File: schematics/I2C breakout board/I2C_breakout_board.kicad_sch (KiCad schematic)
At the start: 22 parts, among them J1 Conn_01x01_Pin, J10 Conn_01x01_Pin, J11 Conn_01x01_Pin, J12 Conn_01x01_Pin, J13 Conn_01x01_Pin, J14 Conn_01x01_Pin, J15 Conn_01x01_Pin, J16 Conn_01x01_Pin, J17 Conn_01x01_Pin, J2 Conn_01x01_Pin, J3 Conn_01x01_Pin, J4 Conn_01x01_Pin, J5 Conn_01x01_Pin, J6 Conn_01x01_Pin, J7 Conn_01x01_Pin, J8 Conn_01x01_Pin, J9 Conn_01x01_Pin, U1 ENS210-LQFM, U2 OPT4001DTSR

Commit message: testing how to make branches, added dummy text to the schematic
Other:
- note added: "DUMMY TEXT FOR MAKING A BRANCH on github"
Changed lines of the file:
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@@
 		(company "RES-Q-SQUAD")
+	)
+	(text "DUMMY TEXT FOR MAKING A BRANCH\non github\n"
+		(exclude_from_sim no)
+		(at 229.616 59.182 0)
+		(effects
+			(font
+				(size 1.27 1.27)
+			)
+		)
 	)
 	(junction

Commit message: updated schematic
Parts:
- removed J1, J10, J11, J12, J13, J14, J15, J16, J17, J2, J3, J4, J5, J6, J7, J8, J9: Conn_01x01_Pin, Connector_PinHeader_2.54mm:PinHeader_1x01_P2.54mm_Vertical, symbol Connector:Conn_01x01_Pin
- added J1, J2: Conn_01x07_Pin, Connector_PinHeader_2.54mm:PinHeader_1x07_P2.54mm_Vertical, symbol Connector:Conn_01x07_Pin
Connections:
- net +3.3V: now also J1.1 (Pin_1), J2.7 (Pin_7)
- net GND: now also J2.1 (Pin_1), J2.6 (Pin_6)
- net SCL: now reaches U1.2 (SCL)
- net SCL: now also U2.5 (SCL), J1.2 (Pin_2)
- net SDA: now reaches U1.3 (SDA)
- net SDA: now also U2.8 (SDA), J2.2 (Pin_2)
- net U3_DI: now reaches U3.4 (DI)
- net U3_DI: now also J1.7 (Pin_7)
- net U3_RO: now reaches U3.1 (RO)
- net U3_RO: now also J1.4 (Pin_4)
- net U2_ADDR: now reaches U2.2 (ADDR)
- net U2_ADDR: now also J1.3 (Pin_3)
- net U2_INT: now reaches U2.7 (INT)
- net U2_INT: now also J2.3 (Pin_3)
- net U3_DE: now reaches U3.3 (DE)
- net U3_DE: now also J1.6 (Pin_6)
- net U3_/RE: now reaches U3.2 (/RE)
- net U3_/RE: now also J1.5 (Pin_5)
- net U3__B: now reaches U3.7 (B)
- net U3__B: now also J2.4 (Pin_4)
- net U3_A: now reaches U3.6 (A)
- net U3_A: now also J2.5 (Pin_5)
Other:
- moved on the sheet: C1, C2

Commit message: finalized PCB for breakout board
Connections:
- net +3.3V: now also J2.4 (Pin_4); no longer J2.7 (Pin_7)
- net GND: now also J1.2 (Pin_2), J2.7 (Pin_7); no longer J2.1 (Pin_1), J2.6 (Pin_6)
- net SCL: now also J2.2 (Pin_2); no longer J1.2 (Pin_2)
- net SDA: now also J2.1 (Pin_1); no longer J2.2 (Pin_2)
- net U2_ADDR: now also J2.3 (Pin_3); no longer J1.3 (Pin_3)
- net U2_INT: now also J1.3 (Pin_3); no longer J2.3 (Pin_3)
- net U3_A: now also J2.6 (Pin_6); no longer J2.5 (Pin_5)
- net U3__B: now also J2.5 (Pin_5); no longer J2.4 (Pin_4)

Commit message: .
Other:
- note removed: "DUMMY TEXT FOR MAKING A BRANCH on github"
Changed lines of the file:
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@@
 		(company "RES-Q-SQUAD")
-	)
-	(text "DUMMY TEXT FOR MAKING A BRANCH\non github\n"
-		(exclude_from_sim no)
-		(at 229.616 59.182 0)
-		(effects
-			(font
-				(size 1.27 1.27)
-			)
-		)
 	)
 	(junction

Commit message: final version of air sensors breakout board
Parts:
- removed J1, J2: Conn_01x07_Pin, Connector_PinHeader_2.54mm:PinHeader_1x07_P2.54mm_Vertical, symbol Connector:Conn_01x07_Pin
- added C3: 0.1u, Capacitor_SMD:C_0805_2012Metric_Pad1.18x1.45mm_HandSolder, symbol Device:C
- added J3: 54602-908LF, 54602_908LF_footprints:CONN8_2-908LF_AMP, symbol 2026-10-21_23-02-14:54602-908LF
- added J4, J5: Conn_01x05_Pin, Connector_PinHeader_2.54mm:PinHeader_1x05_P2.54mm_Vertical, symbol Connector:Conn_01x05_Pin
- added R1: 120, Resistor_SMD:R_0805_2012Metric_Pad1.20x1.40mm_HandSolder, symbol Device:R_US
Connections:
- net +3.3V: now also C3.2, J3.7, J3.8, J5.4 (Pin_4)
- net GND: now also C3.1, J3.1, J3.2, J4.2 (Pin_2)
- net SCL: now also J5.5 (Pin_5)
- net SDA: now also J4.1 (Pin_1)
- net U2_ADDR: now also J5.3 (Pin_3)
- net U2_INT: now also J5.2 (Pin_2)
- net U3_DE: now also J4.4 (Pin_4)
- net U3_DI: now also J4.5 (Pin_5)
- net U3_RO: now also J5.1 (Pin_1)
- net U3_/RE: now also J4.3 (Pin_3)
- net U3_A: no longer names the net of U3.6 (A)
- net U3_A: now also J3.4, R1.1
- net U3__B: no longer names the net of U3.7 (B)
- net U3__B: now also J3.5, R1.2
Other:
- moved on the sheet: C1, C2, U1, U2, U3

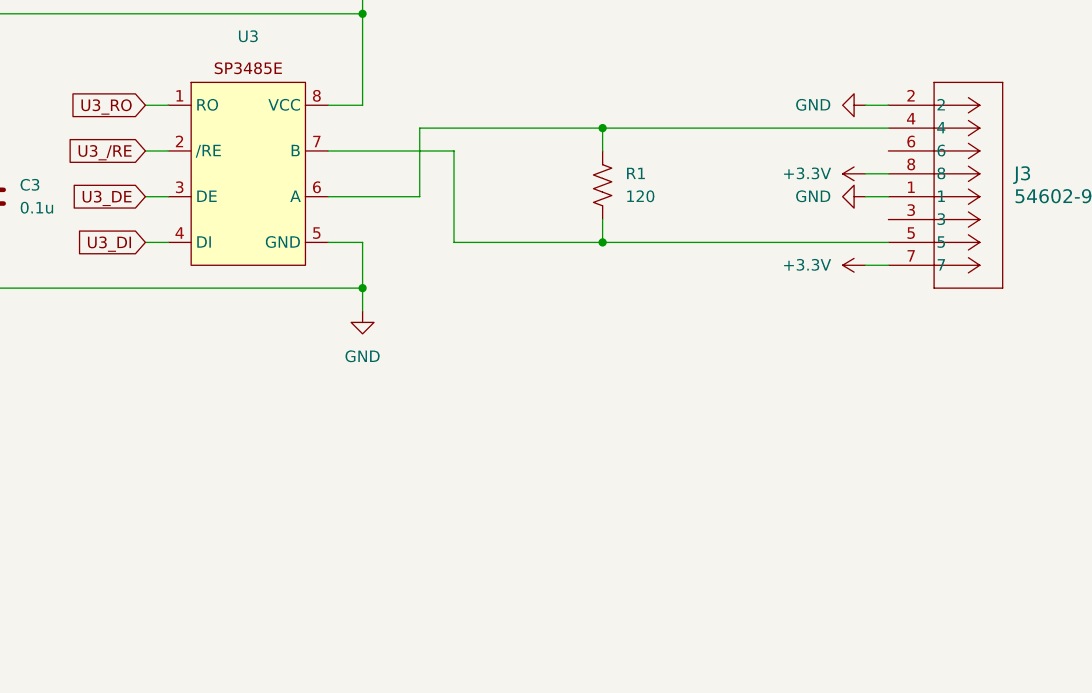
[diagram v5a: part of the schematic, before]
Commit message: added PMOS to turn off power to RJ45 connector
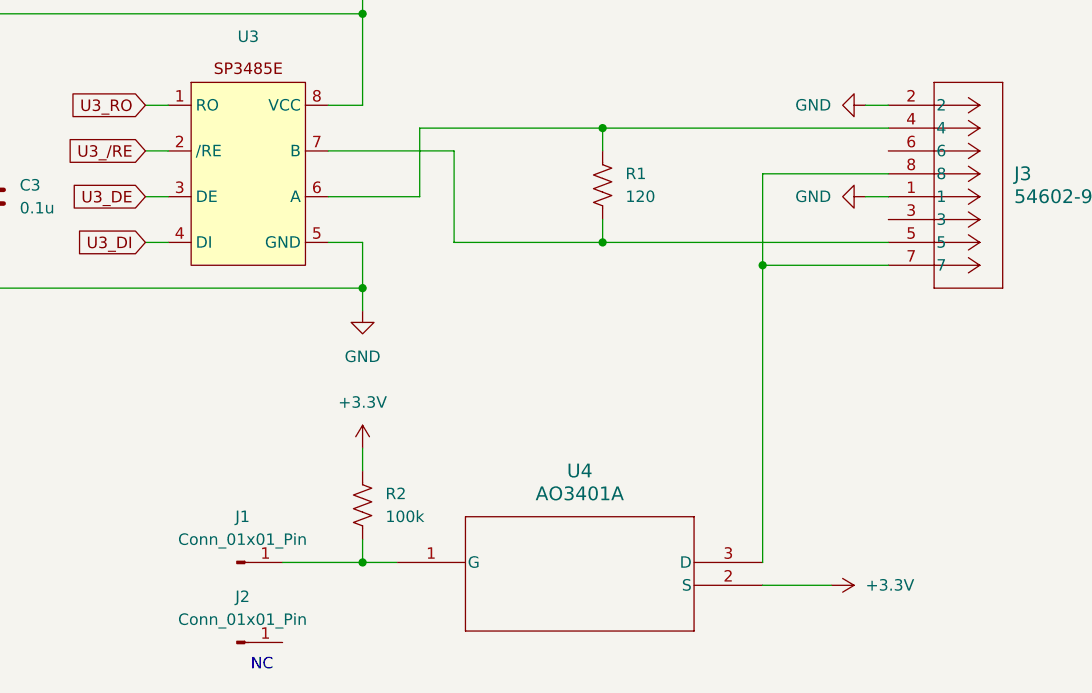
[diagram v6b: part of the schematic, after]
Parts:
- added J1, J2: Conn_01x01_Pin, Connector_PinHeader_2.54mm:PinHeader_1x01_P2.54mm_Vertical, symbol Connector:Conn_01x01_Pin
- added R2: 100k, Resistor_SMD:R_0805_2012Metric_Pad1.20x1.40mm_HandSolder, symbol Device:R_US
- added U4: AO3401A, AO3401A_footprints:SOT-23-3L_AOS-M, symbol 2026-10-23_19-01-03:AO3401A
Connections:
- net +3.3V: now also R2.1, U4.2 (S); no longer J3.7, J3.8
- new net: J1.1 (Pin_1), R2.2, U4.1 (G)
- new net: J3.7, J3.8, U4.3 (D)
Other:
- note added: "NC"

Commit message: Final changes to pcbs before ordering
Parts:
- renumbered J4 to J1, J5 to J2, J1 to J4, J2 to J5, U4 to Q1
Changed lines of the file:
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@@
 		(dnp no)
 		(fields_autoplaced yes)
-		(property "Reference" "J1"
+		(property "Reference" "J4"
 			(at 156.845 123.19 0)
 			(show_name no)
@@
 			(project "I2C_breakout_board"
 				(path "/be40f0ea-e108-4aba-ae64-f07137c70a25"
-					(reference "J1")
+					(reference "J4")
 					(unit 1)
 				)
@@
 		(dnp no)
 		(fields_autoplaced yes)
-		(property "Reference" "J4"
+		(property "Reference" "J1"
 			(at 160.655 31.75 0)
 			(show_name no)
@@
 			(project "I2C_breakout_board"
 				(path "/be40f0ea-e108-4aba-ae64-f07137c70a25"
-					(reference "J4")
+					(reference "J1")
 					(unit 1)
 				)
@@
 		(dnp no)
 		(fields_autoplaced yes)
-		(property "Reference" "J2"
+		(property "Reference" "J5"
 			(at 156.845 132.08 0)
 			(show_name no)
@@
 			(project "I2C_breakout_board"
 				(path "/be40f0ea-e108-4aba-ae64-f07137c70a25"
-					(reference "J2")
+					(reference "J5")
 					(unit 1)
 				)
@@
 		(dnp no)
 		(fields_autoplaced yes)
-		(property "Reference" "U4"
+		(property "Reference" "Q1"
 			(at 194.31 118.11 0)
 			(show_name no)
@@
 			(project "I2C_breakout_board"
 				(path "/be40f0ea-e108-4aba-ae64-f07137c70a25"
-					(reference "U4")
+					(reference "Q1")
 					(unit 1)
 				)
@@
 		(in_pos_files yes)
 		(dnp no)
-		(property "Reference" "J5"
+		(property "Reference" "J2"
 			(at 202.946 30.988 0)
 			(show_name no)
@@
 			(project "I2C_breakout_board"
 				(path "/be40f0ea-e108-4aba-ae64-f07137c70a25"
-					(reference "J5")
-					(unit 1)
-				)
+					(reference "J2")
+					(unit 1)
+				)
